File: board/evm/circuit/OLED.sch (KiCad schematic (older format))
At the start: 1 part

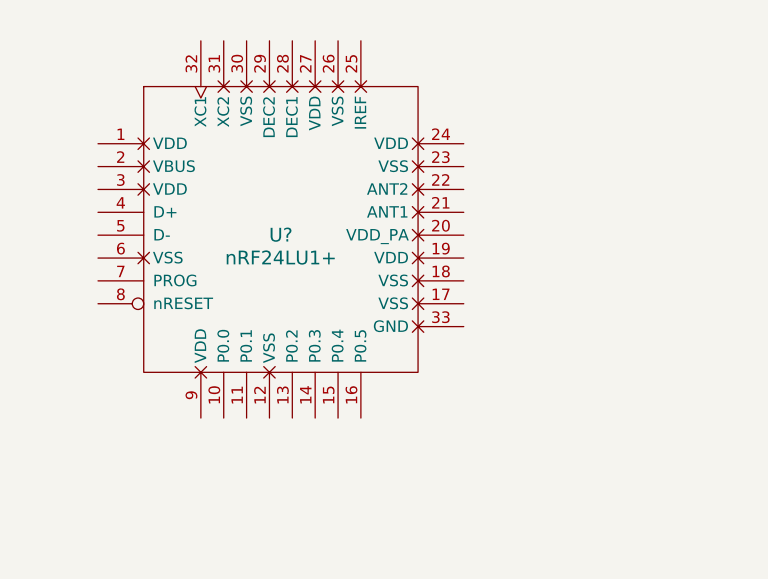
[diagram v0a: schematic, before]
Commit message: add more schs
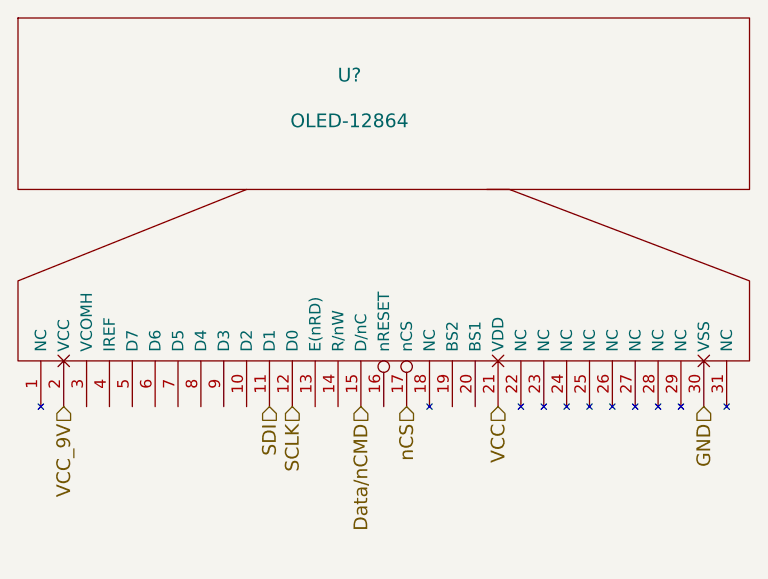
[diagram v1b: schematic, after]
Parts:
- removed U?: nRF24LU1+, symbol nRF24LU1+
- added U?: OLED-12864, symbol OLED-12864
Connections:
- new net Data/nCMD: U?.15 (D/nC)
- new net GND: U?.30 (VSS)
- new net SCLK: U?.12 (D0)
- new net SDI: U?.11 (D1)
- new net VCC: U?.21 (VDD)
- new net VCC_9V: U?.2 (VCC)
- new net nCS: U?.17 (nCS)
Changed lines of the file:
@@
 $Descr A4 11693 8268
 encoding utf-8
-Sheet 7 11
+Sheet 10 11
 Title ""
 Date ""
@@
 $EndDescr
 $Comp
-L nRF24LU1+ U?
-U 1 1 5754763F
-P 3500 2850
-F 0 "U?" H 3500 2850 60  0000 C CNN
-F 1 "nRF24LU1+" H 3500 2750 60  0000 C CNN
-F 2 "" H 3500 2850 60  0000 C CNN
-F 3 "" H 3500 2850 60  0000 C CNN
-	1    3500 2850
+L OLED-12864 U?
+U 1 1 5759530E
+P 3900 2550
+F 0 "U?" H 3800 2950 60  0000 C CNN
+F 1 "OLED-12864" H 3800 2750 60  0000 C CNN
+F 2 "" H 2850 1850 60  0000 C CNN
+F 3 "" H 2850 1850 60  0000 C CNN
+	1    3900 2550
 	1    0    0    -1
 $EndComp
+Text HLabel 2550 3600 3    60   Input ~ 0
+VCC_9V
+Text HLabel 5350 3600 3    60   Input ~ 0
+GND
+Text HLabel 4450 3600 3    60   Input ~ 0
+VCC
+Text HLabel 3850 3600 3    60   Input ~ 0
+Data/nCMD
+Text HLabel 4050 3600 3    60   Input ~ 0
+nCS
+Text HLabel 3550 3600 3    60   Input ~ 0
+SCLK
+Text HLabel 3450 3600 3    60   Input ~ 0
+SDI
 $EndSCHEMATC

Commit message: battery sch nearly done
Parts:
- added C? (x2): 0.1uF, symbol C_Small
- added C? (x2): 20uF, symbol C_Small
- added D?: D_SM340A, symbol D_Schottky
- added L?: 3.3uH, symbol INDUCTOR
- added R?: R10K, symbol R
- added R?: R88K, symbol R
- added R?: R12K, symbol R
- added U?: FP6291, symbol FP6291
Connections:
- net GND: now also C?.2, C?.2, C?.2, C?.2, R?.2, R?.2, U?.2 (GND)
- net VCC renamed +3V3
- net +3V3: now also C?.1, C?.1, L?.1, U?.4 (EN), U?.5 (VCC)
- net VCC_9V renamed +12V
- net +12V: now also C?.1, C?.1, D?.1 (K), R?.1
- new net: D?.2 (A), L?.2, U?.1 (LX)
- new net: R?.1, R?.2, U?.3 (FB)
- new net: R?.1, U?.6 (OC)
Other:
- note added: "FIXME!"

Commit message: working on leak current detection
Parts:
- removed C? (x2): 0.1uF, symbol C_Small
- removed C? (x2): 20uF, symbol C_Small
- removed D?: D_SM340A, symbol D_Schottky
- removed L?: 3.3uH, symbol INDUCTOR
- removed R?: R10K, symbol R
- removed R?: R88K, symbol R
- removed R?: R12K, symbol R
- removed U?: FP6291, symbol FP6291
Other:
- note removed: "FIXME!"

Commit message: evm sch design finished
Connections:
- net GND: now also U?.19 (BS2), U?.20 (BS1)
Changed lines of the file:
@@
 LIBS:contrib
 LIBS:valves
-LIBS:stm8
-LIBS:stm32
-LIBS:74xgxx
-LIBS:ac-dc
-LIBS:actel
 LIBS:Altera
-LIBS:analog_devices
-LIBS:battery_management
-LIBS:bbd
-LIBS:brooktre
-LIBS:cmos_ieee
-LIBS:dc-dc
-LIBS:diode
-LIBS:elec-unifil
-LIBS:ESD_Protection
-LIBS:ftdi
-LIBS:gennum
-LIBS:graphic
-LIBS:hc11
-LIBS:ir
-LIBS:Lattice
-LIBS:logo
-LIBS:maxim
-LIBS:microchip_dspic33dsc
-LIBS:microchip_pic10mcu
-LIBS:microchip_pic12mcu
-LIBS:microchip_pic16mcu
-LIBS:microchip_pic18mcu
-LIBS:microchip_pic32mcu
-LIBS:motor_drivers
-LIBS:msp430
-LIBS:nordicsemi
-LIBS:nxp_armmcu
-LIBS:onsemi
-LIBS:Oscillators
-LIBS:powerint
-LIBS:Power_Management
-LIBS:pspice
-LIBS:references
-LIBS:relays
-LIBS:rfcom
-LIBS:sensors
-LIBS:silabs
-LIBS:supertex
-LIBS:switches
-LIBS:transf
-LIBS:ttl_ieee
-LIBS:video
-LIBS:Worldsemi
-LIBS:Xicor
-LIBS:Zilog
+LIBS:my_kicad
 LIBS:oh-my-keyboard-cache
 EELAYER 25 0
@@
 $Descr A3 16535 11693
 encoding utf-8
-Sheet 10 11
+Sheet 10 12
 Title ""
 Date ""
@@
 Wire Wire Line
 	1650 900  1650 800
+$Comp
+L GND #PWR?
+U 1 1 57662DD2
+P 4250 3700
+F 0 "#PWR?" H 4250 3450 50  0001 C CNN
+F 1 "GND" H 4250 3550 50  0000 C CNN
+F 2 "" H 4250 3700 50  0000 C CNN
+F 3 "" H 4250 3700 50  0000 C CNN
+	1    4250 3700
+	1    0    0    -1
+$EndComp
+Wire Wire Line
+	4250 3700 4250 3600
+Wire Wire Line
+	4350 3600 4350 3650
+Wire Wire Line
+	4350 3650 4250 3650
+Connection ~ 4250 3650
 $EndSCHEMATC

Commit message: working on qc3
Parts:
- gave numbers to parts that had none: 1
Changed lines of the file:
@@
 LIBS:contrib
 LIBS:valves
+LIBS:stm8
+LIBS:stm32
+LIBS:74xgxx
+LIBS:ac-dc
+LIBS:actel
 LIBS:Altera
-LIBS:my_kicad
+LIBS:analog_devices
+LIBS:battery_management
+LIBS:bbd
+LIBS:brooktre
+LIBS:cmos_ieee
+LIBS:dc-dc
+LIBS:diode
+LIBS:elec-unifil
+LIBS:ESD_Protection
+LIBS:ftdi
+LIBS:gennum
+LIBS:graphic
+LIBS:hc11
+LIBS:ir
+LIBS:Lattice
+LIBS:logo
+LIBS:maxim
+LIBS:microchip_dspic33dsc
+LIBS:microchip_pic10mcu
+LIBS:microchip_pic12mcu
+LIBS:microchip_pic16mcu
+LIBS:microchip_pic18mcu
+LIBS:microchip_pic32mcu
+LIBS:motor_drivers
+LIBS:msp430
+LIBS:nordicsemi
+LIBS:nxp_armmcu
+LIBS:onsemi
 LIBS:Oscillators
+LIBS:powerint
+LIBS:Power_Management
+LIBS:pspice
+LIBS:references
+LIBS:relays
+LIBS:rfcom
+LIBS:sensors
+LIBS:silabs
+LIBS:supertex
+LIBS:switches
+LIBS:transf
+LIBS:ttl_ieee
+LIBS:video
+LIBS:Worldsemi
+LIBS:Xicor
+LIBS:Zilog
 LIBS:oh-my-keyboard-cache
 EELAYER 25 0
@@
 $EndDescr
 $Comp
-L OLED-12864 U?
+L OLED-12864 U10
 U 1 1 5759530E
 P 3900 2550
-F 0 "U?" H 3800 2950 60  0000 C CNN
+F 0 "U10" H 3800 2950 60  0000 C CNN
 F 1 "OLED-12864" H 3800 2750 60  0000 C CNN
 F 2 "" H 2850 1850 60  0000 C CNN
@@
 GND
 $Comp
-L GND #PWR?
+L GND #PWR096
 U 1 1 575AD12D
 P 5350 3600
-F 0 "#PWR?" H 5350 3350 50  0001 C CNN
+F 0 "#PWR096" H 5350 3350 50  0001 C CNN
 F 1 "GND" H 5350 3450 50  0000 C CNN
 F 2 "" H 5350 3600 50  0000 C CNN
@@
 $EndComp
 $Comp
-L +3V3 #PWR?
+L +3V3 #PWR097
 U 1 1 575AD192
 P 4450 3600
-F 0 "#PWR?" H 4450 3450 50  0001 C CNN
+F 0 "#PWR097" H 4450 3450 50  0001 C CNN
 F 1 "+3V3" H 4450 3740 50  0000 C CNN
 F 2 "" H 4450 3600 50  0000 C CNN
@@
 $EndComp
 $Comp
-L +3V3 #PWR?
+L +3V3 #PWR098
 U 1 1 575AD1C6
 P 1650 1200
-F 0 "#PWR?" H 1650 1050 50  0001 C CNN
+F 0 "#PWR098" H 1650 1050 50  0001 C CNN
 F 1 "+3V3" H 1650 1340 50  0000 C CNN
 F 2 "" H 1650 1200 50  0000 C CNN
@@
 	1650 1350 1650 1200
 $Comp
-L GND #PWR?
+L GND #PWR099
 U 1 1 575AD218
 P 1650 1700
-F 0 "#PWR?" H 1650 1450 50  0001 C CNN
+F 0 "#PWR099" H 1650 1450 50  0001 C CNN
 F 1 "GND" H 1650 1550 50  0000 C CNN
 F 2 "" H 1650 1700 50  0000 C CNN
@@
 	1650 1550 1650 1700
 $Comp
-L +12V #PWR?
+L +12V #PWR0100
 U 1 1 575AE2B2
 P 2550 3800
-F 0 "#PWR?" H 2550 3650 50  0001 C CNN
+F 0 "#PWR0100" H 2550 3650 50  0001 C CNN
 F 1 "+12V" H 2550 3940 50  0000 C CNN
 F 2 "" H 2550 3800 50  0000 C CNN
@@
 VCC_12V
 $Comp
-L +12V #PWR?
+L +12V #PWR0101
 U 1 1 575C0189
 P 1650 800
-F 0 "#PWR?" H 1650 650 50  0001 C CNN
+F 0 "#PWR0101" H 1650 650 50  0001 C CNN
 F 1 "+12V" H 1650 940 50  0000 C CNN
 F 2 "" H 1650 800 50  0000 C CNN
@@
 	1650 900  1650 800
 $Comp
-L GND #PWR?
+L GND #PWR0102
 U 1 1 57662DD2
 P 4250 3700
-F 0 "#PWR?" H 4250 3450 50  0001 C CNN
+F 0 "#PWR0102" H 4250 3450 50  0001 C CNN
 F 1 "GND" H 4250 3550 50  0000 C CNN
 F 2 "" H 4250 3700 50  0000 C CNN
